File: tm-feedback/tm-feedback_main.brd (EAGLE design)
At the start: 60.1 x 40.3 mm, 45 parts

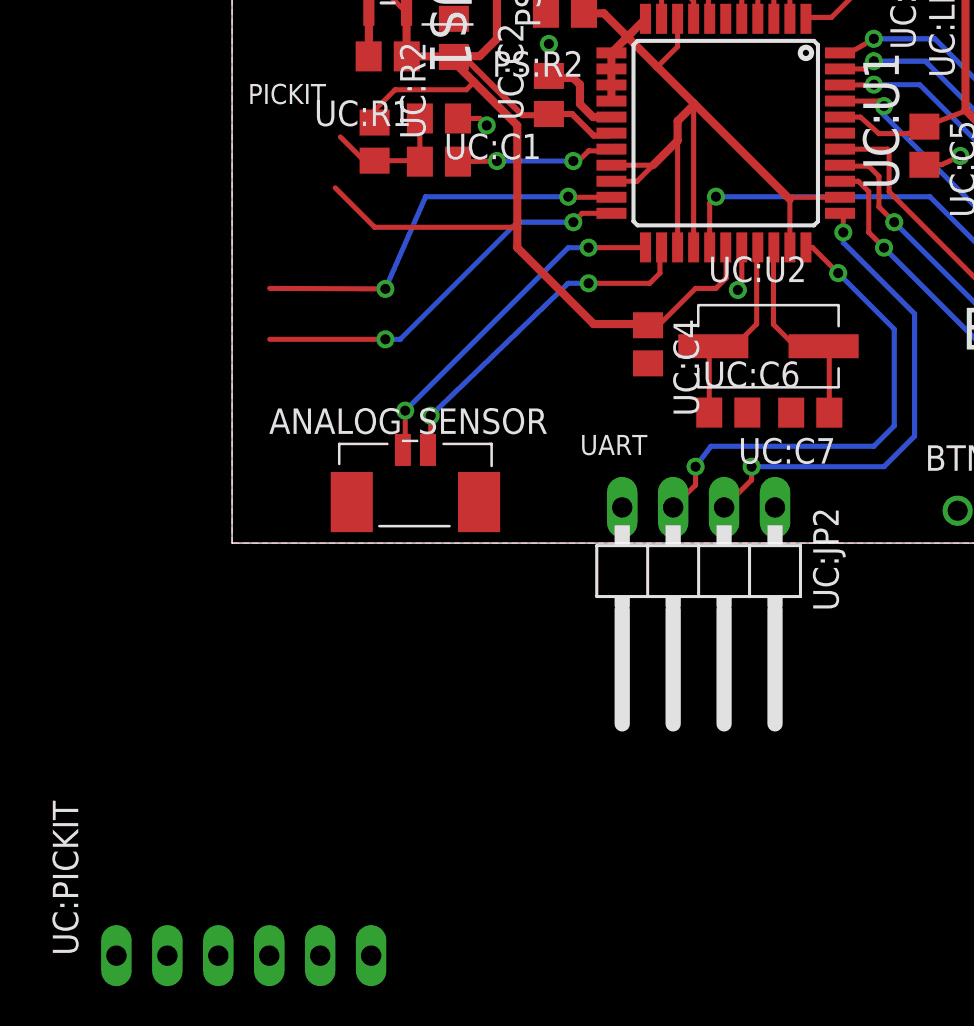
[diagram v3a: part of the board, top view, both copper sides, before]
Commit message: Replace headers in schematic and board, no design rule errors
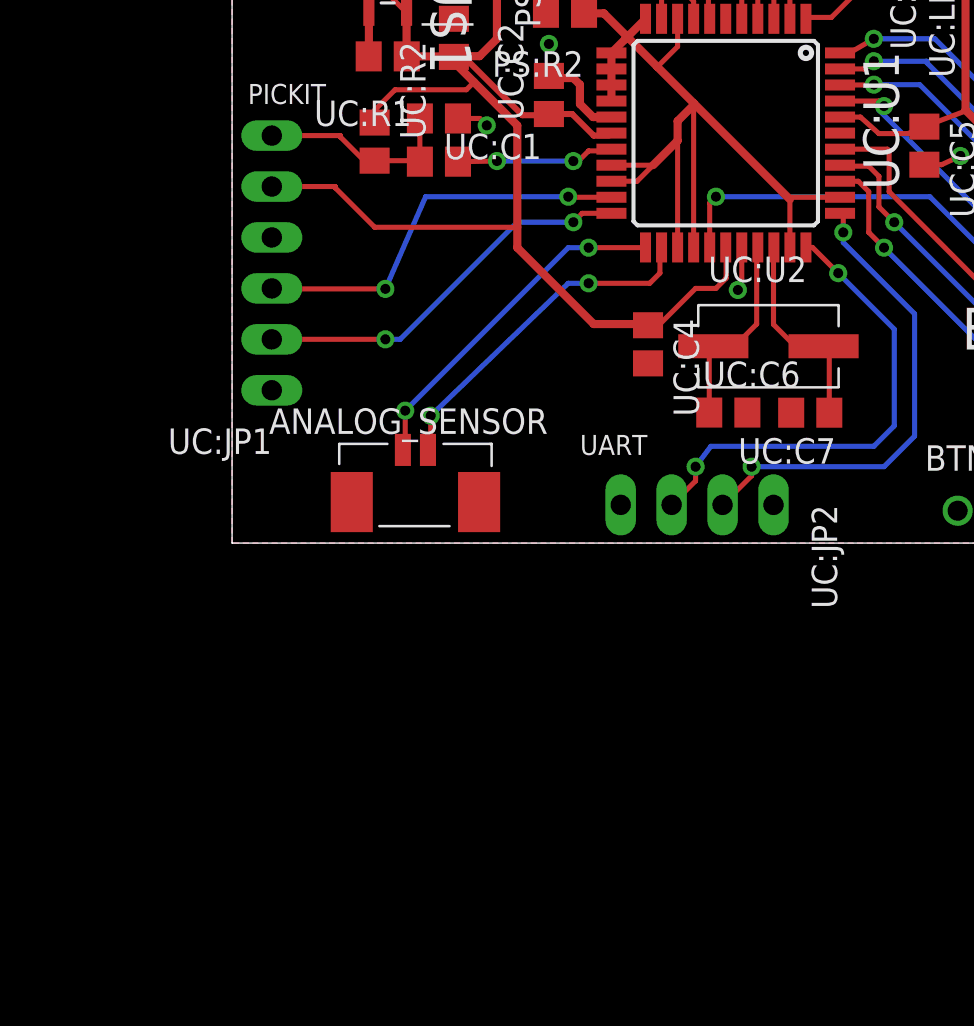
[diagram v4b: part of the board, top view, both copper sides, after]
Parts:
- removed UC:PICKIT: JP1, tactile-music:1X06/90
- added UC:JP1: PICKIT, tactile-music:1X06/90
- UC:JP2: device pinhead:1X04/90 -> tactile-music:1X04/90
- moved UC:JP2 0.15 mm to (23.2, -1.91)
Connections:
- net +3V3: now also UC:JP1.5; no longer UC:PICKIT.5
- net GND: now also UC:JP1.4; no longer UC:PICKIT.4
- net UC:!MCLR: now also UC:JP1.6; no longer UC:PICKIT.6
- net UC:PGC: now also UC:JP1.2; no longer UC:PICKIT.2
- net UC:PGD: now also UC:JP1.3; no longer UC:PICKIT.3
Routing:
- net UC:!MCLR: track 6.65 -> 10.1 mm
- net +3V3: track 148.5 -> 151.7 mm
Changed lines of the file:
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@@
 <layer number="21" name="tPlace" color="7" fill="1" visible="yes" active="yes"/>
 <layer number="22" name="bPlace" color="7" fill="1" visible="no" active="yes"/>
-<layer number="23" name="tOrigins" color="15" fill="1" visible="no" active="yes"/>
-<layer number="24" name="bOrigins" color="15" fill="1" visible="no" active="yes"/>
+<layer number="23" name="tOrigins" color="15" fill="1" visible="yes" active="yes"/>
+<layer number="24" name="bOrigins" color="15" fill="1" visible="yes" active="yes"/>
 <layer number="25" name="tNames" color="7" fill="1" visible="no" active="yes"/>
 <layer number="26" name="bNames" color="7" fill="1" visible="no" active="yes"/>
@@
 <attribute name="VALUE" x="42.475" y="1.506" size="1.27" layer="27"/>
 </element>
-<element name="UC:JP2" library="pinhead" package="1X04/90" value="UART_PC" x="23.2664" y="-2.032" smashed="yes" rot="R180">
-<attribute name="NAME" x="28.9814" y="1.778" size="1.27" layer="25" ratio="10" rot="R270"/>
-<attribute name="VALUE" x="16.2814" y="2.413" size="1.27" layer="27" rot="R270"/>
-</element>
 <element name="PS:U$1" library="tactile-music" package="SOT95P270X145-5N" value="MCP1824T-3302E/OT" x="7.762" y="27.824" smashed="yes" rot="R270">
 <attribute name="MPN" value="MCP1824T-3302E/OT" x="7.762" y="27.824" size="1.778" layer="27" rot="R270" display="off"/>
@@
 </element>
 <element name="BTN:PAIRING_SW" library="tactile-music" package="THRU-TACTILE-BTN" value="MC32881_TACTILE" x="38.6828" y="1.614" smashed="yes" rot="MR0"/>
-<element name="UC:PICKIT" library="tactile-music" package="1X06/90" value="JP1" x="0.5842" y="-16.764"/>
+<element name="UC:JP1" library="tactile-music" package="1X06/90" value="PICKIT" x="-1.8288" y="13.97" rot="R90"/>
+<element name="UC:JP2" library="tactile-music" package="1X04/90" value="UART_PC" x="23.1902" y="-1.905" rot="R180"/>
 </elements>
 <signals>
@@
 <contactref element="UC:LED1" pad="C"/>
 <contactref element="BTN:U1" pad="3"/>
-<contactref element="UC:JP2" pad="1"/>
 <contactref element="UC:R7" pad="2"/>
 <contactref element="BT:U$1" pad="24"/>
@@
 <wire x1="17.018" y1="23.1902" x2="15.9058" y2="23.1902" width="0.4064" layer="1"/>
 <wire x1="15.9058" y1="23.1902" x2="15.8" y2="23.296" width="0.4064" layer="1"/>
-<contactref element="UC:PICKIT" pad="4"/>
-<wire x1="47.8562" y1="31.2774" x2="56.37" y2="24.5036" width="0" layer="19" extent="1-1"/>
-<wire x1="45.47" y1="24.5036" x2="47.8562" y2="31.2774" width="0" layer="19" extent="1-1"/>
-<wire x1="41.308" y1="24.712" x2="45.47" y2="24.5036" width="0" layer="19" extent="1-1"/>
-<wire x1="41.338" y1="18.722" x2="41.308" y2="24.712" width="0" layer="19" extent="1-1"/>
-<wire x1="42.238" y1="14.658" x2="42.926" y2="18.288" width="0" layer="19" extent="1-16"/>
-<wire x1="45.47" y1="13.0036" x2="42.926" y2="13.97" width="0" layer="19" extent="1-1"/>
-<wire x1="36.322" y1="19.304" x2="41.338" y2="18.722" width="0" layer="19" extent="1-1"/>
-<wire x1="30.318" y1="20.444" x2="34.524" y2="18.868" width="0" layer="19" extent="1-1"/>
-<wire x1="39.1448" y1="8.0856" x2="41.434" y2="14.658" width="0" layer="19" extent="1-1"/>
-<wire x1="40.06" y1="6.146" x2="39.1448" y2="8.0856" width="0" layer="19" extent="1-1"/>
-<wire x1="36.1828" y1="1.614" x2="40.06" y2="6.146" width="0" layer="19" extent="1-1"/>
-<wire x1="25.418" y1="14.744" x2="30.318" y2="20.444" width="0" layer="19" extent="1-1"/>
-<wire x1="20.744" y1="8.962" x2="25.2222" y2="12.6238" width="0" layer="19" extent="1-1"/>
-<wire x1="25.696" y1="6.508" x2="20.744" y2="8.962" width="0" layer="19" extent="1-1"/>
-<wire x1="27.882" y1="6.502" x2="25.696" y2="6.508" width="0" layer="19" extent="1-1"/>
-<wire x1="27.0764" y1="1.778" x2="27.882" y2="6.502" width="0" layer="19" extent="1-1"/>
-<wire x1="48.56" y1="2.072" x2="41.656" y2="5.334" width="0" layer="19" extent="1-16"/>
-<wire x1="33.49" y1="27.73" x2="30.318" y2="20.444" width="0" layer="19" extent="1-1"/>
-<wire x1="24.618" y1="26.144" x2="30.318" y2="20.444" width="0" layer="19" extent="1-1"/>
-<wire x1="23.8576" y1="30.7236" x2="24.618" y2="26.144" width="0" layer="19" extent="1-1"/>
-<wire x1="26.911" y1="35.548" x2="23.8576" y2="30.7236" width="0" layer="19" extent="1-1"/>
-<wire x1="18.918" y1="21.244" x2="24.618" y2="26.144" width="0" layer="19" extent="1-1"/>
-<wire x1="15.7988" y1="24.892" x2="15.8" y2="23.824" width="0" layer="19" extent="1-1"/>
-<wire x1="15.652" y1="26.32" x2="15.7988" y2="24.892" width="0" layer="19" extent="1-1"/>
-<wire x1="12.7" y1="20.828" x2="15.8" y2="23.296" width="0" layer="19" extent="1-1"/>
-<wire x1="11.062" y1="26.144" x2="15.652" y2="26.444" width="0" layer="19" extent="1-1"/>
-<wire x1="7.762" y1="29.1956" x2="11.062" y2="26.144" width="0" layer="19" extent="1-1"/>
-<wire x1="9.918" y1="32.946" x2="7.762" y2="29.1956" width="0" layer="19" extent="1-1"/>
-<wire x1="9.5212" y1="36.8528" x2="9.918" y2="32.946" width="0" layer="19" extent="1-1"/>
-<wire x1="14.668" y1="31.136" x2="15.652" y2="26.444" width="0" layer="19" extent="1-1"/>
-<wire x1="56.37" y1="13.0036" x2="45.47" y2="13.0036" width="0" layer="19" extent="1-1"/>
-<wire x1="56.8884" y1="9.645" x2="56.37" y2="13.0036" width="0" layer="19" extent="1-1"/>
-<wire x1="1.8542" y1="-20.574" x2="27.0764" y2="1.778" width="0" layer="19" extent="1-1"/>
+<contactref element="UC:JP1" pad="4"/>
+<contactref element="UC:JP2" pad="1"/>
 </signal>
 <signal name="BT:N$6">
@@
 <wire x1="9.316" y1="19.07" x2="9.366" y2="19.02" width="0.254" layer="1"/>
 <wire x1="9.366" y1="19.02" x2="9.366" y2="21.174" width="0.254" layer="1"/>
-<contactref element="UC:PICKIT" pad="6"/>
-<wire x1="6.9342" y1="-20.574" x2="6.604" y2="19.05" width="0" layer="19" extent="1-1"/>
+<contactref element="UC:JP1" pad="6"/>
+<wire x1="1.9812" y1="20.32" x2="5.4" y2="20.32" width="0.254" layer="1"/>
+<wire x1="5.4" y1="20.32" x2="5.4" y2="20.254" width="0.254" layer="1"/>
 </signal>
 <signal name="UC:PGD">
@@
 <wire x1="9.652" y1="17.272" x2="7.6454" y2="12.6746" width="0.254" layer="16"/>
 <via x="7.6454" y="12.6746" extent="1-16" drill="0.5"/>
-<wire x1="7.6454" y1="12.6746" x2="1.876" y2="12.7" width="0.254" layer="1"/>
-<contactref element="UC:PICKIT" pad="3"/>
-<wire x1="1.876" y1="12.7" x2="-0.6858" y2="-20.574" width="0" layer="19" extent="1-1"/>
+<contactref element="UC:JP1" pad="3"/>
+<wire x1="7.6454" y1="12.6746" x2="1.9812" y2="12.6746" width="0.254" layer="1"/>
+<wire x1="1.9812" y1="12.6746" x2="1.9812" y2="12.7" width="0.254" layer="1"/>
 </signal>
 <signal name="UC:PGC">
@@
 <via x="17.018" y="16.002" extent="1-16" drill="0.5"/>
 <via x="7.6454" y="10.16" extent="1-16" drill="0.5"/>
-<wire x1="7.6454" y1="10.16" x2="1.876" y2="10.16" width="0.254" layer="1"/>
 <wire x1="7.6454" y1="10.16" x2="8.382" y2="10.16" width="0.254" layer="16"/>
 <wire x1="8.382" y1="10.16" x2="14.224" y2="16.002" width="0.254" layer="16"/>
 <wire x1="14.224" y1="16.002" x2="17.018" y2="16.002" width="0.254" layer="16"/>
-<contactref element="UC:PICKIT" pad="2"/>
-<wire x1="1.876" y1="10.16" x2="-3.2258" y2="-20.574" width="0" layer="19" extent="1-1"/>
+<contactref element="UC:JP1" pad="2"/>
+<wire x1="7.6454" y1="10.16" x2="1.9812" y2="10.16" width="0.254" layer="1"/>
 </signal>
 <signal name="UC:N$3">
@@
 <wire x1="12.3422" y1="24.2802" x2="11.0982" y2="24.2802" width="0.4064" layer="1"/>
 <wire x1="11.0982" y1="24.2802" x2="11.062" y2="24.244" width="0.254" layer="1"/>
-<contactref element="UC:PICKIT" pad="5"/>
-<wire x1="4.3942" y1="-20.574" x2="18.034" y2="10.922" width="0" layer="19" extent="1-1"/>
+<contactref element="UC:JP1" pad="5"/>
+<wire x1="1.9812" y1="17.78" x2="5.146" y2="17.78" width="0.254" layer="1"/>
+<wire x1="5.146" y1="17.78" x2="5.146" y2="17.714" width="0.254" layer="1"/>
 </signal>
 <signal name="BTN:N$2">
@@
 <signal name="UC:UART2_RX">
 <contactref element="UC:U1" pad="33"/>
-<contactref element="UC:JP2" pad="3"/>
 <wire x1="28.618" y1="14.744" x2="28.944" y2="14.744" width="0.254" layer="1"/>
 <wire x1="28.944" y1="14.744" x2="30.226" y2="13.462" width="0.254" layer="1"/>
@@
 <wire x1="23.876" y1="4.826" x2="23.114" y2="3.81" width="0.254" layer="16"/>
 <via x="23.114" y="3.81" extent="1-16" drill="0.5"/>
-<wire x1="23.114" y1="3.81" x2="23.114" y2="2.8956" width="0.254" layer="1"/>
-<wire x1="23.114" y1="2.8956" x2="21.9964" y2="1.778" width="0.254" layer="1"/>
 <wire x1="33.02" y1="10.668" x2="33.02" y2="5.842" width="0.254" layer="16"/>
 <wire x1="33.02" y1="5.842" x2="32.004" y2="4.826" width="0.254" layer="16"/>
 <wire x1="32.004" y1="4.826" x2="23.876" y2="4.826" width="0.254" layer="16"/>
+<contactref element="UC:JP2" pad="3"/>
+<wire x1="23.114" y1="3.81" x2="23.114" y2="3.0988" width="0.254" layer="1"/>
+<wire x1="23.114" y1="3.0988" x2="21.9202" y2="1.905" width="0.254" layer="1"/>
 </signal>
 <signal name="UC:UART2_TX">
 <contactref element="UC:U1" pad="34"/>
-<contactref element="UC:JP2" pad="2"/>
 <wire x1="30.318" y1="16.444" x2="30.48" y2="16.444" width="0.254" layer="1"/>
 <wire x1="30.48" y1="16.444" x2="30.48" y2="15.494" width="0.254" layer="1"/>
@@
 <wire x1="30.48" y1="14.986" x2="34.036" y2="11.43" width="0.254" layer="16"/>
 <via x="25.908" y="3.81" extent="1-16" drill="0.5"/>
-<wire x1="25.908" y1="3.81" x2="25.908" y2="3.1496" width="0.254" layer="1"/>
-<wire x1="25.908" y1="3.1496" x2="24.5364" y2="1.778" width="0.254" layer="1"/>
 <wire x1="34.036" y1="11.43" x2="34.036" y2="5.334" width="0.254" layer="16"/>
 <wire x1="34.036" y1="5.334" x2="32.512" y2="3.81" width="0.254" layer="16"/>
 <wire x1="32.512" y1="3.81" x2="25.908" y2="3.81" width="0.254" layer="16"/>
+<contactref element="UC:JP2" pad="2"/>
+<wire x1="25.908" y1="3.81" x2="25.908" y2="3.3528" width="0.254" layer="1"/>
+<wire x1="25.908" y1="3.3528" x2="24.4602" y2="1.905" width="0.254" layer="1"/>
 </signal>
 <signal name="N$2">

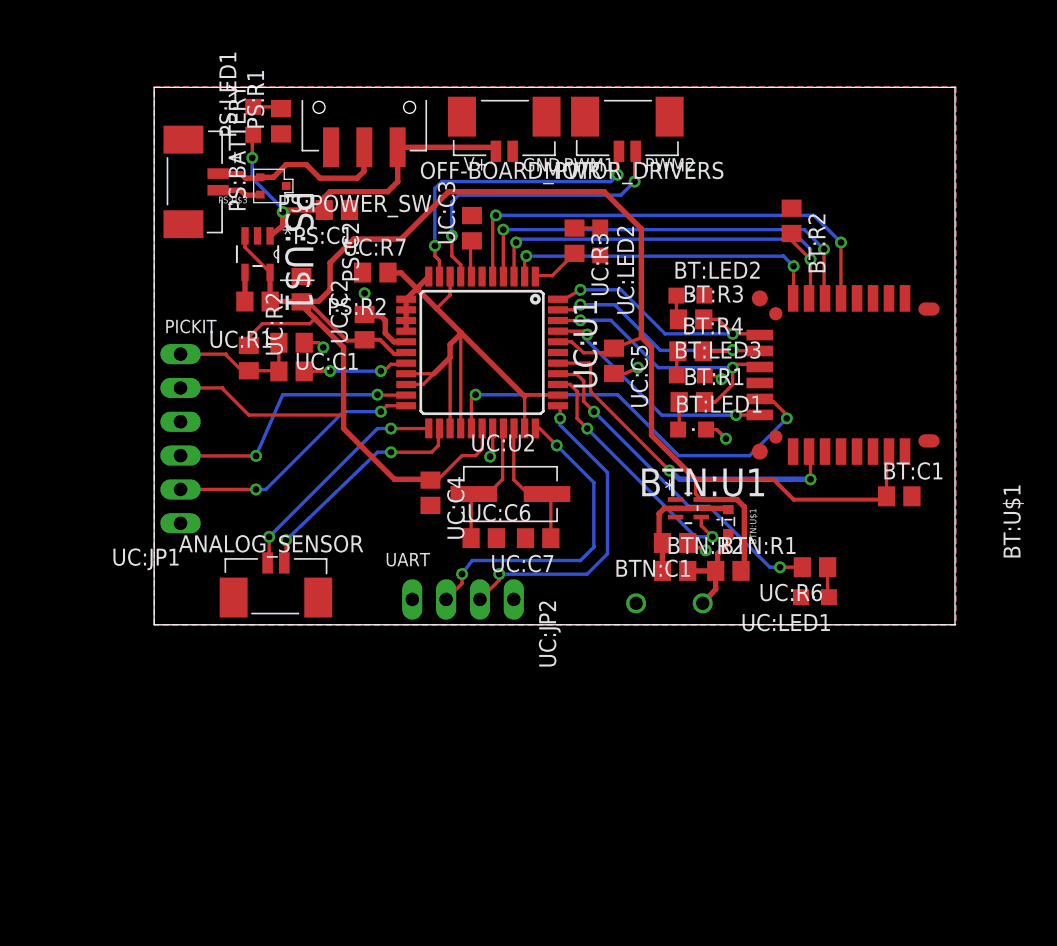
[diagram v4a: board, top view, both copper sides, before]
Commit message: Add labels, icon
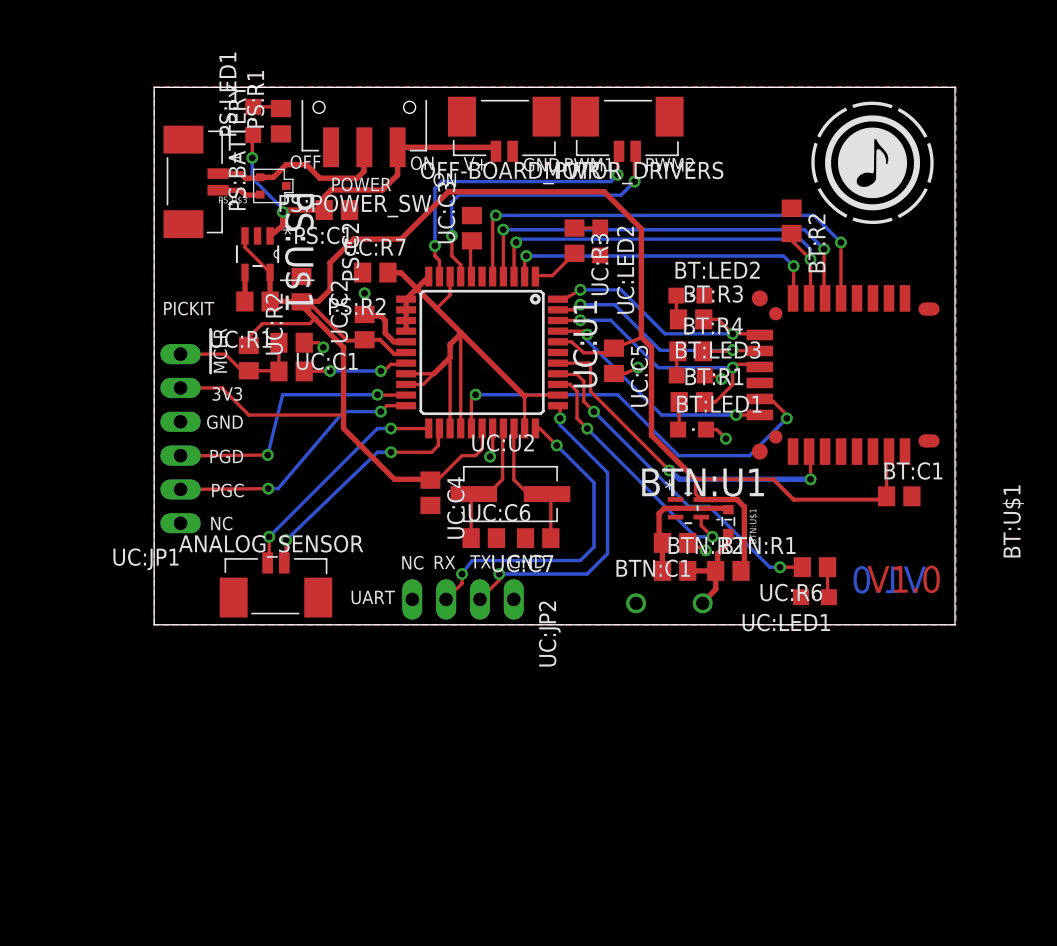
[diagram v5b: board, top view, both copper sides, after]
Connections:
- net PS:N$5 renamed PS:PWRGD
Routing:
- net UC:PGD: track 20.0 -> 20.5 mm
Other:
- board text added: "!MCLR"
- board text added: "3V3"
- board text added: "NC"
- board text added: "OFF"
- board text added: "ON"
- board text added: "PGC"
- board text added: "PGD"
- board text added: "POWER"
- board text added: "RX"
- board text added: "TX"
- board text added: "V1.0"
